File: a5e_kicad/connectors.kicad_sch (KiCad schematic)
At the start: 2 parts, among them P1 SODIMM-200, P2 DF12NB-40DS-0.5V_51_

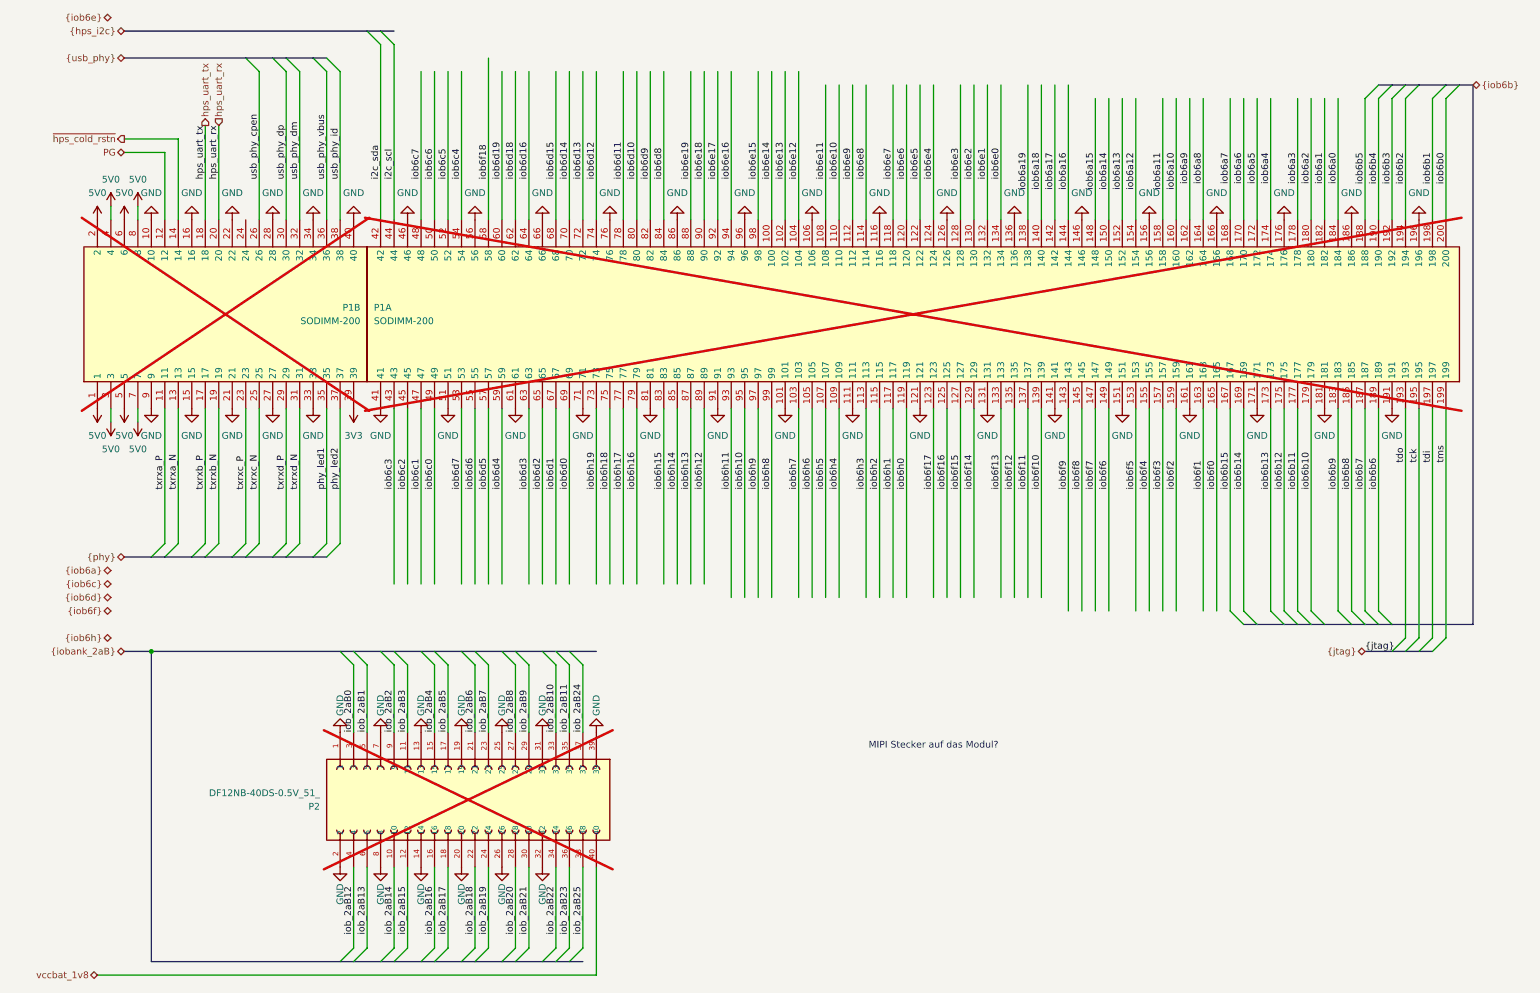
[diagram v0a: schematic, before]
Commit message: Remove leftover SODIMM P1 and DF12 P2 connectors
- Remove P1 (SODIMM-200) and P2 (DF12NB-40DS) and all wiring, labels,
  bus entries and power symbols that only served them
- Remove the dead sheet pins they left behind on the top-level sheet:
  Connectors PG / ~{hps_cold_rstn} / hps_uart_tx / hps_uart_rx,
  HPS hps_uart_tx / hps_uart_rx, and vccbat_1v8 on the FPGA power,
  Connectors and IOBANK6gh sheets (vccbat only went to P2; U7 VCCBAT is
  tied to 1V8). The HPS console is on U42/J10.
- Drop the stale SODIMM/DF12 symbol cache entries

Netlist compared before/after: no other connectivity or net names
changed. ERC 583 -> 542.

Co-Authored-By: Claude Opus 5.5 <noreply@anthropic.com>
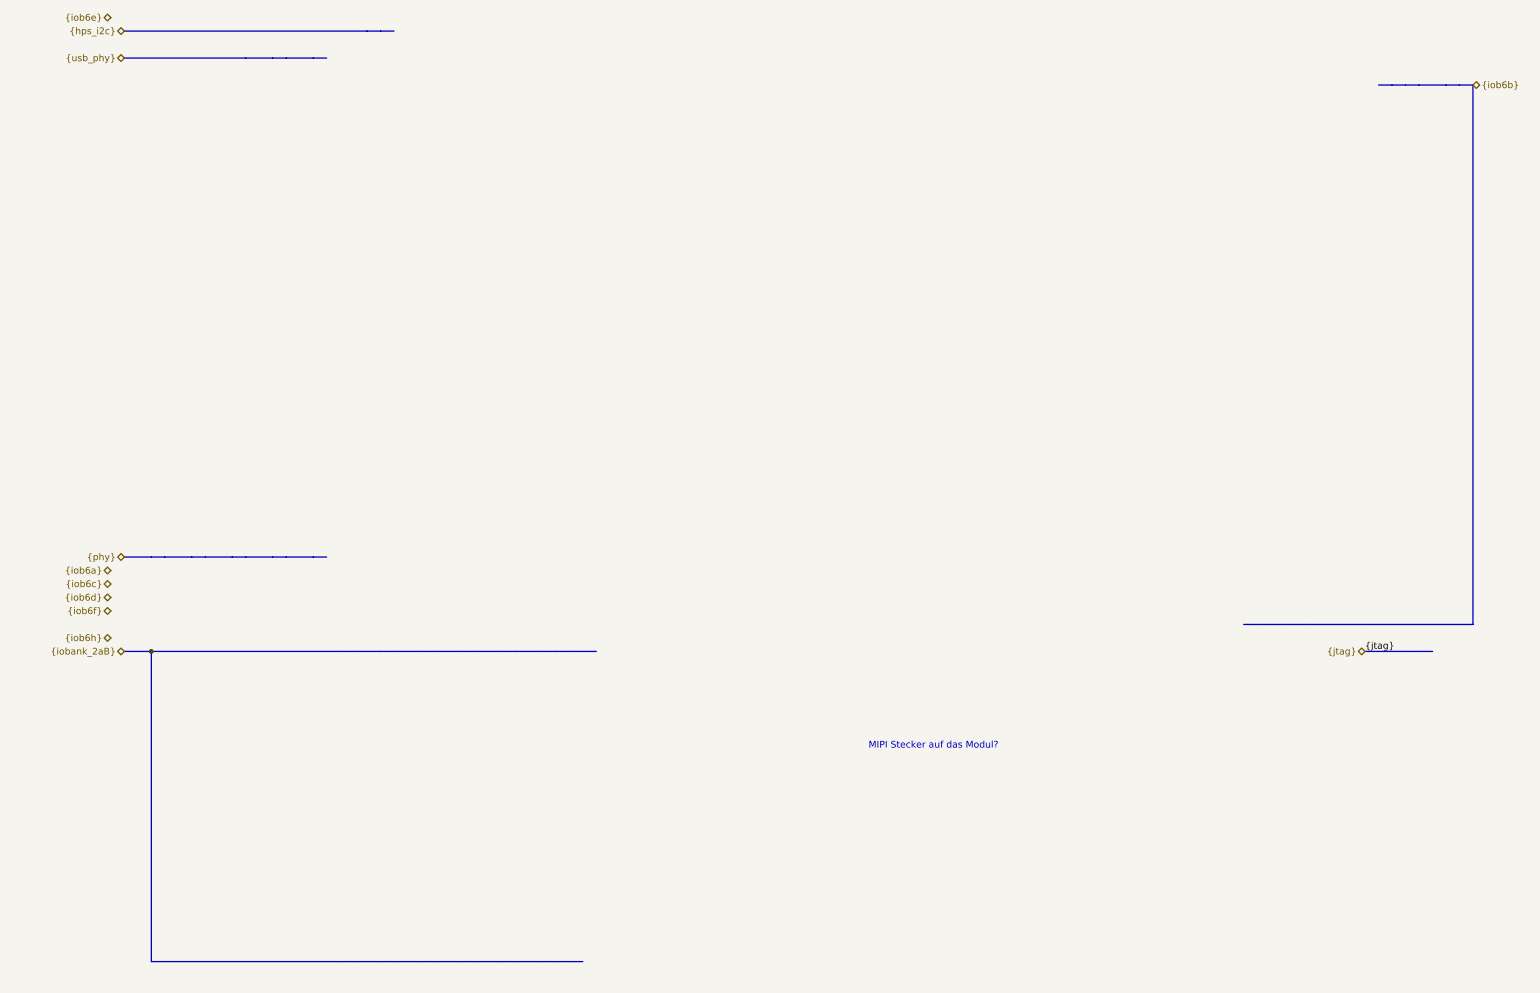
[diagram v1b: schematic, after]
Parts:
- removed P1: SODIMM-200, PCAD_import:DIMM-SO200, symbol Connector:SODIMM-200
- removed P2: DF12NB-40DS-0.5V_51_, DF12NB-40DS-0.5V_51_:HRS_DF12NB-40DS-0.5V_51_, symbol DF12NB-40DS-0.5V_51_:DF12NB-40DS-0.5V_51_
